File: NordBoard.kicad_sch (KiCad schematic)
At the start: 97 parts, among them SW1 SW_Push, SW10 SW_Push, SW11 SW_Push, SW12 SW_Push, SW13 SW_Push, SW14 SW_Push, SW15 SW_Push, SW16 SW_Push, SW17 SW_Push, SW18 SW_Push, SW19 SW_Push, SW2 SW_Push, SW20 SW_Push, SW21 SW_Push, SW22 SW_Push, SW23 SW_Push, SW24 SW_Push, SW25 SW_Push, SW26 SW_Push, SW27 SW_Push, SW28 SW_Push, SW29 SW_Push, SW3 SW_Push, SW30 SW_Push, SW31 SW_Push, SW32 SW_Push, SW33 SW_Push, SW34 SW_Push, SW35 SW_Push, SW36 SW_Push, SW37 SW_Push, SW38 SW_Push, SW39 SW_Push, SW4 SW_Push, SW40 SW_Push, SW41 SW_Push, SW42 SW_Push, SW5 SW_Push, SW6 SW_Push, SW7 SW_Push, SW8 SW_Push, SW9 SW_Push, U1 XIAO-RP2040-DIP, U2 XIAO-RP2040-DIP

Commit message: major feat: completely restructure project, new switches, no more path hardcoding
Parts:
- U1, U2: footprint Seeed Studio XIAO Series Library:XIAO-RP2040-DIP -> kicad_care_package:XIAO-RP2040-DIP
- renumbered D11 to D10, D12 to D11, D13 to D12, D14 to D13, D15 to D14, D16 to D15, D17 to D16, D18 to D17, D19 to D18, D20 to D19, D21 to D20, D22 to D21, D23 to D22, D24 to D23, D26 to D24, D27 to D25, D28 to D26, D29 to D27, D30 to D28, D31 to D29, D32 to D30, D33 to D31, D34 to D32, D35 to D33, D36 to D34, D37 to D35, D38 to D36, D39 to D37, D40 to D38, D41 to D39, D5 to D4, D42 to D40, D6 to D5, D4 to D50, D25 to D51, D7 to D6, D8 to D7, D9 to D8, D10 to D9, SW11 to SW10, SW12 to SW11, SW13 to SW12, SW14 to SW13, SW15 to SW14, SW16 to SW15, SW17 to SW16, SW18 to SW17, SW19 to SW18, SW20 to SW19, SW21 to SW20, SW22 to SW21, SW23 to SW22, SW24 to SW23, SW26 to SW24, SW27 to SW25, SW28 to SW26, SW29 to SW27, SW30 to SW28, SW31 to SW29, SW32 to SW30, SW33 to SW31, SW34 to SW32, SW35 to SW33, SW36 to SW34, SW37 to SW35, SW38 to SW36, SW39 to SW37, SW40 to SW38, SW41 to SW39, SW5 to SW4, SW42 to SW40, SW6 to SW5, SW4 to SW50, SW25 to SW51, SW7 to SW6, SW8 to SW7, SW9 to SW8, SW10 to SW9

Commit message: feat: new journal, fix some errors, usb-c interconnect, new edge cuts and so much more
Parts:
- added P1, P2: USB_C_Plug_USB2.0, symbol Connector:USB_C_Plug_USB2.0
- B1, B2, B3, B4, B5: footprint PCM_marbastlib-various:mousebites_2mm -> kicad_care_package:mousebites_2mm
- U1, U2: symbol Seeed_Studio_XIAO_Series:XIAO-RP2040-DIP -> XIAO_RP2040:MOUDLE-SEEEDUINO-XIAO
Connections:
- net COL0: no longer SW21.1, SW22.1, SW23.1, SW50.1, SW51.1, U2.2 (GPIO27/ADC1/A1)
- net COL1: no longer SW24.1, SW25.1, SW26.1, U2.3 (GPIO28/ADC2/A2)
- net COL2: no longer SW27.1, SW28.1, SW29.1, U2.4 (GPIO29/ADC3/A3)
- net COL3: now also SW16.1; no longer SW30.1, SW31.1, SW32.1, U2.5 (GPIO6/SDA)
- net COL4: now also SW20.1; no longer SW16.1, SW33.1, SW34.1, SW35.1, SW36.1, U2.6 (GPIO7/SCL)
- net COL5: now also SW50.1; no longer SW20.1, SW37.1, SW38.1, SW39.1, SW40.1, U2.7 (GPIO0/TX)
- net ROW0: no longer D21.1 (K), D24.1 (K), D27.1 (K), D30.1 (K), D33.1 (K), D37.1 (K), U2.11 (GPIO3/MOSI)
- net ROW1: no longer D22.1 (K), D25.1 (K), D28.1 (K), D31.1 (K), D34.1 (K), D38.1 (K), U2.10 (GPIO4/MISO)
- net ROW2: no longer D23.1 (K), D26.1 (K), D29.1 (K), D32.1 (K), D35.1 (K), D39.1 (K), U2.9 (GPIO2/SCK)
- net ROW3: no longer D36.1 (K), D40.1 (K), D51.1 (K), U2.8 (GPIO1/RX)
- net INTERCON: now reaches U2.1 (PA02_A0_D0)
- net INTERCON: now also U1.1 (PA02_A0_D0)
- new net: P1.A1 (GND), P1.A12 (GND), P1.B1 (GND), P1.B12 (GND)
- new net: P1.A4 (VBUS), P1.A9 (VBUS), P1.B4 (VBUS), P1.B9 (VBUS)
- new net: P2.A1 (GND), P2.A12 (GND), P2.B1 (GND), P2.B12 (GND)
- new net: P2.A4 (VBUS), P2.A9 (VBUS), P2.B4 (VBUS), P2.B9 (VBUS)
- new net COL10: SW33.1, SW34.1, SW35.1, SW40.1, U2.6 (PA9_A5_D5_SCL)
- new net COL11: SW37.1, SW38.1, SW39.1, SW51.1, U2.7 (PB08_A6_D6_TX)
- new net COL6: SW21.1, SW22.1, SW23.1, U2.2 (PA4_A1_D1)
- new net COL7: SW24.1, SW25.1, SW26.1, U2.3 (PA10_A2_D2)
- new net COL8: SW27.1, SW28.1, SW29.1, U2.4 (PA11_A3_D3)
- new net COL9: SW30.1, SW31.1, SW32.1, SW36.1, U2.5 (PA8_A4_D4_SDA)
- new net ROW4: D21.1 (K), D24.1 (K), D27.1 (K), D30.1 (K), D33.1 (K), D37.1 (K), U2.11 (PA6_A10_D10_MOSI)
- new net ROW5: D22.1 (K), D25.1 (K), D28.1 (K), D31.1 (K), D34.1 (K), D38.1 (K), U2.10 (PA5_A9_D9_MISO)
- new net ROW6: D23.1 (K), D26.1 (K), D29.1 (K), D32.1 (K), D35.1 (K), D39.1 (K), U2.9 (PA7_A8_D8_SCK)
- new net ROW7: D36.1 (K), D40.1 (K), D51.1 (K), U2.8 (PB09_A7_D7_RX)
- no-connect marks 8 -> 4
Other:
- note added: "USB-C Interconnect"
- moved on the sheet: D16, D20, D21, D22, D23, D24, D25, D26, D27, D28, D29, D30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

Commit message: feat: interconnect cable, new journal
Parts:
- removed P2: USB_C_Plug_USB2.0, symbol Connector:USB_C_Plug_USB2.0
- added P2: USB_C_Plug_USB2.0, Connector_USB:USB_C_Receptacle_GCT_USB4105-xx-A_16P_TopMnt_Horizontal, symbol Connector:USB_C_Receptacle_USB2.0_16P
- added R1: 4.7k, Resistor_SMD:R_0805_2012Metric_Pad1.20x1.40mm_HandSolder, symbol Device:R
- P1: footprint (none) -> Connector_USB:USB_C_Receptacle_GCT_USB4105-xx-A_16P_TopMnt_Horizontal; symbol Connector:USB_C_Plug_USB2.0 -> Connector:USB_C_Receptacle_USB2.0_16P
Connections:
- net GND_L: now reaches P1.A1 (GND), P1.A12 (GND), P1.B1 (GND), P1.B12 (GND)
- net GND_L: now also P1.SH (SHIELD), U1.13 (GND)
- net 5V_L: now reaches P1.A4 (VBUS), P1.A9 (VBUS), P1.B4 (VBUS), P1.B9 (VBUS)
- net 5V_L: now also U1.14 (5V)
- net INTERCON_L: now reaches P1.A6 (D+)
- net INTERCON_L: now also P1.B6 (D+), U1.1 (PA02_A0_D0), R1.1
- net GND_R: now reaches U2.13 (GND)
- net GND_R: now also P2.A1 (GND), P2.A12 (GND), P2.B1 (GND), P2.B12 (GND), P2.SH (SHIELD)
- net 5V_R: now reaches U2.14 (5V)
- net 5V_R: now also P2.A4 (VBUS), P2.A9 (VBUS), P2.B4 (VBUS), P2.B9 (VBUS)
- net 3V3_L: now reaches U1.12 (3V3)
- net 3V3_L: now also R1.2
- net INTERCON renamed INTERCON_R
- net INTERCON_R: now also P2.A6 (D+), P2.B6 (D+); no longer U1.1 (PA02_A0_D0)
- no-connect marks 4 -> 13
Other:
- note added: "Interconnect Resistor"
- moved on the sheet: B1, B2, B3, B4, B5, H4, H5, H6, U1

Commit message: feat: new journal, finish PCB
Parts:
- removed B5: MouseBite, kicad_care_package:mousebites_2mm, symbol Mechanical:MouseBite
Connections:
- net COL0: now also U1.6 (PA9_A5_D5_SCL); no longer U1.2 (PA4_A1_D1)
- net COL1: now also U1.7 (PB08_A6_D6_TX); no longer U1.3 (PA10_A2_D2)
- net COL2: now also U1.11 (PA6_A10_D10_MOSI); no longer U1.4 (PA11_A3_D3)
- net COL3: now also U1.10 (PA5_A9_D9_MISO); no longer U1.5 (PA8_A4_D4_SDA)
- net COL4: now also U1.9 (PA7_A8_D8_SCK); no longer U1.6 (PA9_A5_D5_SCL)
- net COL5: now also U1.8 (PB09_A7_D7_RX); no longer U1.7 (PB08_A6_D6_TX)
- net ROW0: now also U1.2 (PA4_A1_D1); no longer U1.11 (PA6_A10_D10_MOSI)
- net ROW1: now also U1.3 (PA10_A2_D2); no longer U1.10 (PA5_A9_D9_MISO)
- net ROW2: now also U1.4 (PA11_A3_D3); no longer U1.9 (PA7_A8_D8_SCK)
- net ROW3: now also U1.5 (PA8_A4_D4_SDA); no longer U1.8 (PB09_A7_D7_RX)
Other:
- moved on the sheet: B1, B2, B3, B4
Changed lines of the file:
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@@
 		)
 	)
-	(label "COL0"
+	(label "ROW0"
 		(at 17.78 116.84 0)
 		(effects
@@
 		)
 	)
-	(label "COL2"
+	(label "ROW2"
 		(at 17.78 121.92 0)
 		(effects
@@
 		)
 	)
-	(label "COL4"
+	(label "COL0"
 		(at 17.78 127 0)
 		(effects
@@
 		)
 	)
-	(label "COL3"
+	(label "ROW3"
 		(at 17.78 124.46 0)
 		(effects
@@
 		)
 	)
-	(label "ROW1"
+	(label "COL3"
 		(at 82.55 124.46 180)
 		(effects
@@
 		)
 	)
-	(label "ROW2"
+	(label "COL4"
 		(at 82.55 127 180)
 		(effects
@@
 		)
 	)
-	(label "COL5"
+	(label "COL1"
 		(at 17.78 129.54 0)
 		(effects
@@
 		)
 	)
-	(label "ROW3"
+	(label "COL5"
 		(at 82.55 129.54 180)
 		(effects
@@
 		)
 	)
-	(label "ROW0"
+	(label "COL2"
 		(at 82.55 121.92 180)
 		(effects
@@
 		)
 	)
-	(label "COL1"
+	(label "ROW1"
 		(at 17.78 119.38 0)
 		(effects
@@
 	(symbol
 		(lib_id "Mechanical:MouseBite")
-		(at 46.99 147.32 0)
+		(at 54.61 147.32 0)
 		(unit 1)
 		(body_style 1)
@@
 		(dnp no)
 		(property "Reference" "B3"
-			(at 49.53 147.32 0)
+			(at 57.15 147.32 0)
 			(show_name no)
 			(do_not_autoplace no)
@@
 		)
 		(property "Value" "MouseBite"
-			(at 49.53 148.6524 0)
+			(at 57.15 148.6524 0)
 			(hide yes)
 			(show_name no)
@@
 		)
 		(property "Footprint" "kicad_care_package:mousebites_2mm"
-			(at 46.99 147.32 0)
+			(at 54.61 147.32 0)
 			(hide yes)
 			(show_name no)
@@
 		)
 		(property "Datasheet" ""
-			(at 46.99 147.32 0)
+			(at 54.61 147.32 0)
 			(hide yes)
 			(show_name no)
@@
 		)
 		(property "Description" "Mouse bites, break lines"
-			(at 46.99 147.32 0)
+			(at 54.61 147.32 0)
 			(hide yes)
 			(show_name no)
@@
 	(symbol
 		(lib_id "Mechanical:MouseBite")
-		(at 34.29 147.32 0)
+		(at 41.91 147.32 0)
 		(unit 1)
 		(body_style 1)
@@
 		(dnp no)
 		(property "Reference" "B2"
-			(at 36.83 147.32 0)
+			(at 44.45 147.32 0)
 			(show_name no)
 			(do_not_autoplace no)
@@
 		)
 		(property "Value" "MouseBite"
-			(at 36.83 148.6524 0)
+			(at 44.45 148.6524 0)
 			(hide yes)
 			(show_name no)
@@
 		)
 		(property "Footprint" "kicad_care_package:mousebites_2mm"
-			(at 34.29 147.32 0)
+			(at 41.91 147.32 0)
 			(hide yes)
 			(show_name no)
@@
 		)
 		(property "Datasheet" ""
-			(at 34.29 147.32 0)
+			(at 41.91 147.32 0)
 			(hide yes)
 			(show_name no)
@@
 		)
 		(property "Description" "Mouse bites, break lines"
-			(at 34.29 147.32 0)
+			(at 41.91 147.32 0)
 			(hide yes)
 			(show_name no)
@@
 	(symbol
 		(lib_id "Mechanical:MouseBite")
-		(at 20.32 147.32 0)
+		(at 27.94 147.32 0)
 		(unit 1)
 		(body_style 1)
@@
 		(dnp no)
 		(property "Reference" "B1"
-			(at 22.86 147.32 0)
+			(at 30.48 147.32 0)
 			(show_name no)
 			(do_not_autoplace no)
@@
 		)
 		(property "Value" "MouseBite"
-			(at 22.86 148.6524 0)
+			(at 30.48 148.6524 0)
 			(hide yes)
 			(show_name no)
@@
 		)
 		(property "Footprint" "kicad_care_package:mousebites_2mm"
-			(at 20.32 147.32 0)
+			(at 27.94 147.32 0)
 			(hide yes)
 			(show_name no)
@@
 		)
 		(property "Datasheet" ""
-			(at 20.32 147.32 0)
+			(at 27.94 147.32 0)
 			(hide yes)
 			(show_name no)
@@
 		)
 		(property "Description" "Mouse bites, break lines"
-			(at 20.32 147.32 0)
+			(at 27.94 147.32 0)
 			(hide yes)
 			(show_name no)
@@
 	)
 	(symbol
-		(lib_id "Mechanical:MouseBite")
-		(at 74.93 147.32 0)
-		(unit 1)
-		(body_style 1)
-		(exclude_from_sim yes)
-		(in_bom no)
-		(on_board yes)
-		(in_pos_files yes)
-		(dnp no)
-		(property "Reference" "B5"
-			(at 77.47 147.32 0)
-			(show_name no)
-			(do_not_autoplace no)
-			(effects
-				(font
-					(size 1.27 1.27)
-				)
-				(justify left)
-			)
-		)
-		(property "Value" "MouseBite"
-			(at 77.47 148.6524 0)
-			(hide yes)
-			(show_name no)
-			(do_not_autoplace no)
-			(effects
-				(font
-					(size 1.27 1.27)
-				)
-				(justify left)
-			)
-		)
-		(property "Footprint" "kicad_care_package:mousebites_2mm"
-			(at 74.93 147.32 0)
-			(hide yes)
-			(show_name no)
-			(do_not_autoplace no)
-			(effects
-				(font
-					(size 1.27 1.27)
-				)
-			)
-		)
-		(property "Datasheet" ""
-			(at 74.93 147.32 0)
-			(hide yes)
-			(show_name no)
-			(do_not_autoplace no)
-			(effects
-				(font
-					(size 1.27 1.27)
-				)
-			)
-		)
-		(property "Description" "Mouse bites, break lines"
-			(at 74.93 147.32 0)
-			(hide yes)
-			(show_name no)
-			(do_not_autoplace no)
-			(effects
-				(font
-					(size 1.27 1.27)
-				)
-			)
-		)
-		(instances
-			(project "NordBoard"
-				(path "/7cf7f72d-7ab1-4807-b592-339093d5ca44"
-					(reference "B5")
-					(unit 1)
-				)
-			)
-		)
-	)
-	(symbol
 		(lib_id "Device:D")
 		(at 148.59 72.39 90)
@@
 	(symbol
 		(lib_id "Mechanical:MouseBite")
-		(at 60.96 147.32 0)
+		(at 68.58 147.32 0)
 		(unit 1)
 		(body_style 1)
@@
 		(dnp no)
 		(property "Reference" "B4"
-			(at 63.5 147.32 0)
+			(at 71.12 147.32 0)
 			(show_name no)
 			(do_not_autoplace no)
@@
 		)
 		(property "Value" "MouseBite"
-			(at 63.5 148.6524 0)
+			(at 71.12 148.6524 0)
 			(hide yes)
 			(show_name no)
@@
 		)
 		(property "Footprint" "kicad_care_package:mousebites_2mm"
-			(at 60.96 147.32 0)
+			(at 68.58 147.32 0)
 			(hide yes)
 			(show_name no)
@@
 		)
 		(property "Datasheet" ""
-			(at 60.96 147.32 0)
+			(at 68.58 147.32 0)
 			(hide yes)
 			(show_name no)
@@
 		)
 		(property "Description" "Mouse bites, break lines"
-			(at 60.96 147.32 0)
+			(at 68.58 147.32 0)
 			(hide yes)
 			(show_name no)

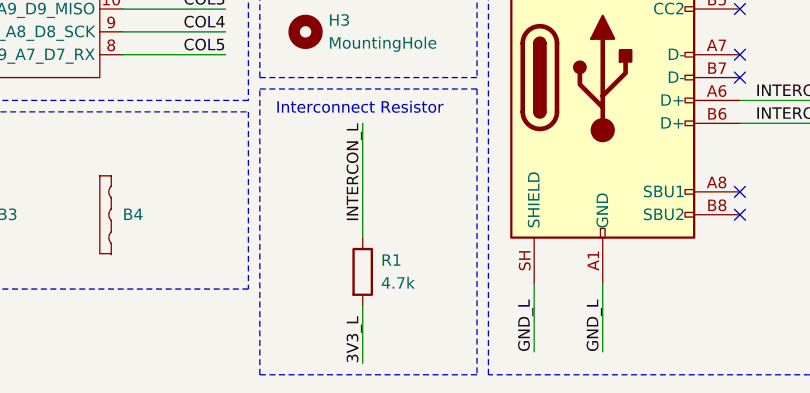
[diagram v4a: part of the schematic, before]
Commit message: feat: switch to 5.1k resistor, fix all 3D models
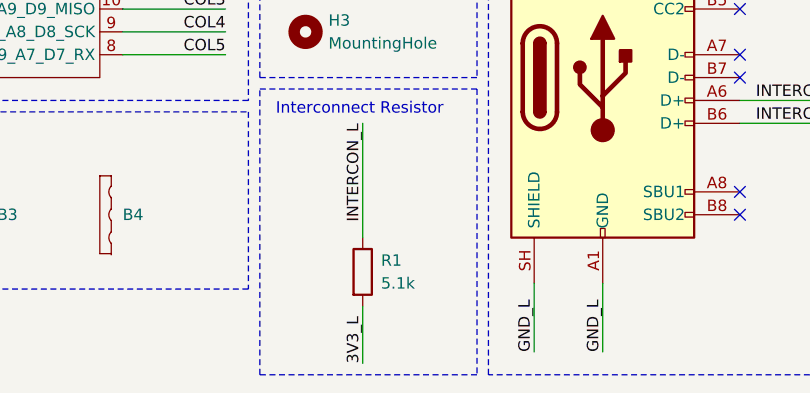
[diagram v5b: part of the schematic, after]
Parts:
- R1: value 4.7k -> 5.1k
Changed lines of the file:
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@@
 			)
 		)
-		(property "Value" "4.7k"
+		(property "Value" "5.1k"
 			(at 99.822 154.94 0)
 			(show_name no)

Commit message: feat: gerbers, new journal, update readme, finish BOM
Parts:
- removed H3, H6: MountingHole, MountingHole:MountingHole_2.2mm_M2, symbol Mechanical:MountingHole
- renumbered H4 to H3, H5 to H4
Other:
- moved on the sheet: R1
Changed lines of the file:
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@@
 	(rectangle
 		(start 86.36 106.68)
-		(end 110.49 132.08)
+		(end 110.49 124.46)
 		(stroke
 			(width 0)
@@
 	)
 	(rectangle
-		(start 86.36 133.35)
-		(end 110.49 165.1)
+		(start 86.36 125.73)
+		(end 110.49 157.48)
 		(stroke
 			(width 0)
@@
 	(rectangle
 		(start 308.61 106.68)
-		(end 332.74 132.08)
+		(end 332.74 124.46)
 		(stroke
 			(width 0)
@@
 	(text "Interconnect Resistor"
 		(exclude_from_sim no)
-		(at 88.138 135.636 0)
+		(at 88.138 128.016 0)
 		(effects
 			(font
@@
 	(wire
 		(pts
-			(xy 97.79 137.16) (xy 97.79 149.86)
+			(xy 97.79 129.54) (xy 97.79 142.24)
 		)
 		(stroke
@@
 	(wire
 		(pts
-			(xy 97.79 157.48) (xy 97.79 163.83)
+			(xy 97.79 149.86) (xy 97.79 156.21)
 		)
 		(stroke
@@
 	)
 	(label "3V3_L"
-		(at 97.79 163.83 90)
+		(at 97.79 156.21 90)
 		(effects
 			(font
@@
 	)
 	(label "INTERCON_L"
-		(at 97.79 137.16 270)
+		(at 97.79 129.54 270)
 		(effects
 			(font
@@
 		(in_pos_files yes)
 		(dnp no)
-		(property "Reference" "H4"
+		(property "Reference" "H3"
 			(at 316.23 113.0299 0)
 			(show_name no)
@@
 			(project "NordBoard"
 				(path "/7cf7f72d-7ab1-4807-b592-339093d5ca44"
-					(reference "H4")
+					(reference "H3")
 					(unit 1)
 				)
@@
 	)
 	(symbol
-		(lib_id "Mechanical:MountingHole")
-		(at 91.44 127 0)
-		(unit 1)
-		(body_style 1)
-		(exclude_from_sim no)
-		(in_bom no)
-		(on_board yes)
-		(in_pos_files yes)
-		(dnp no)
-		(fields_autoplaced yes)
-		(property "Reference" "H3"
-			(at 93.98 125.7299 0)
-			(show_name no)
-			(do_not_autoplace no)
-			(effects
-				(font
-					(size 1.27 1.27)
-				)
-				(justify left)
-			)
-		)
-		(property "Value" "MountingHole"
-			(at 93.98 128.2699 0)
-			(show_name no)
-			(do_not_autoplace no)
-			(effects
-				(font
-					(size 1.27 1.27)
-				)
-				(justify left)
-			)
-		)
-		(property "Footprint" "MountingHole:MountingHole_2.2mm_M2"
-			(at 91.44 127 0)
-			(hide yes)
-			(show_name no)
-			(do_not_autoplace no)
-			(effects
-				(font
-					(size 1.27 1.27)
-				)
-			)
-		)
-		(property "Datasheet" ""
-			(at 91.44 127 0)
-			(hide yes)
-			(show_name no)
-			(do_not_autoplace no)
-			(effects
-				(font
-					(size 1.27 1.27)
-				)
-			)
-		)
-		(property "Description" "Mounting Hole without connection"
-			(at 91.44 127 0)
-			(hide yes)
-			(show_name no)
-			(do_not_autoplace no)
-			(effects
-				(font
-					(size 1.27 1.27)
-				)
-			)
-		)
-		(instances
-			(project "NordBoard"
-				(path "/7cf7f72d-7ab1-4807-b592-339093d5ca44"
-					(reference "H3")
-					(unit 1)
-				)
-			)
-		)
-	)
-	(symbol
 		(lib_id "Device:D")
 		(at 102.87 41.91 90)
@@
 		(in_pos_files yes)
 		(dnp no)
-		(property "Reference" "H5"
+		(property "Reference" "H4"
 			(at 316.23 119.3799 0)
 			(show_name no)
@@
 			(project "NordBoard"
 				(path "/7cf7f72d-7ab1-4807-b592-339093d5ca44"
-					(reference "H5")
+					(reference "H4")
 					(unit 1)
 				)
@@
 	)
 	(symbol
-		(lib_id "Mechanical:MountingHole")
-		(at 311.15 127 0)
-		(unit 1)
-		(body_style 1)
-		(exclude_from_sim no)
-		(in_bom no)
-		(on_board yes)
-		(in_pos_files yes)
-		(dnp no)
-		(property "Reference" "H6"
-			(at 316.23 125.7299 0)
-			(show_name no)
-			(do_not_autoplace no)
-			(effects
-				(font
-					(size 1.27 1.27)
-				)
-				(justify left)
-			)
-		)
-		(property "Value" "MountingHole"
-			(at 316.23 128.2699 0)
-			(show_name no)
-			(do_not_autoplace no)
-			(effects
-				(font
-					(size 1.27 1.27)
-				)
-				(justify left)
-			)
-		)
-		(property "Footprint" "MountingHole:MountingHole_2.2mm_M2"
-			(at 311.15 127 0)
-			(hide yes)
-			(show_name no)
-			(do_not_autoplace no)
-			(effects
-				(font
-					(size 1.27 1.27)
-				)
-			)
-		)
-		(property "Datasheet" ""
-			(at 311.15 127 0)
-			(hide yes)
-			(show_name no)
-			(do_not_autoplace no)
-			(effects
-				(font
-					(size 1.27 1.27)
-				)
-			)
-		)
-		(property "Description" "Mounting Hole without connection"
-			(at 311.15 127 0)
-			(hide yes)
-			(show_name no)
-			(do_not_autoplace no)
-			(effects
-				(font
-					(size 1.27 1.27)
-				)
-			)
-		)
-		(instances
-			(project "NordBoard"
-				(path "/7cf7f72d-7ab1-4807-b592-339093d5ca44"
-					(reference "H6")
-					(unit 1)
-				)
-			)
-		)
-	)
-	(symbol
 		(lib_id "Switch:SW_Push")
 		(at 143.51 55.88 0)
@@
 	(symbol
 		(lib_id "Device:R")
-		(at 97.79 153.67 0)
+		(at 97.79 146.05 0)
 		(unit 1)
 		(body_style 1)
@@
 		(dnp no)
 		(property "Reference" "R1"
-			(at 99.822 152.4 0)
+			(at 99.822 144.78 0)
 			(show_name no)
 			(do_not_autoplace no)
@@
 		)
 		(property "Value" "5.1k"
-			(at 99.822 154.94 0)
+			(at 99.822 147.32 0)
 			(show_name no)
 			(do_not_autoplace no)
@@
 		)
 		(property "Footprint" "Resistor_SMD:R_0805_2012Metric_Pad1.20x1.40mm_HandSolder"
-			(at 96.012 153.67 90)
+			(at 96.012 146.05 90)
 			(hide yes)
 			(show_name no)
@@
 		)
 		(property "Datasheet" ""
-			(at 97.79 153.67 0)
+			(at 97.79 146.05 0)
 			(hide yes)
 			(show_name no)
@@
 		)
 		(property "Description" "Resistor"
-			(at 97.79 153.67 0)
+			(at 97.79 146.05 0)
 			(hide yes)
 			(show_name no)
